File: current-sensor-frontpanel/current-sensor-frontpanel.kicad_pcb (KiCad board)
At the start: 2 copper layers, 98 x 30 mm, 8 parts

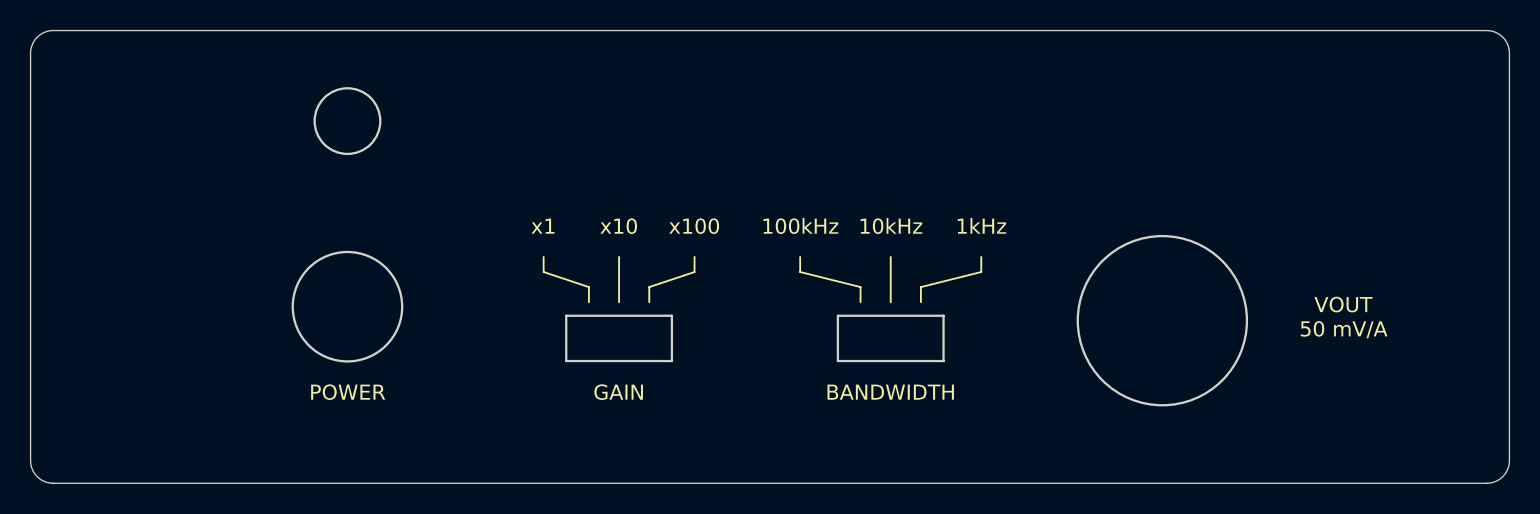
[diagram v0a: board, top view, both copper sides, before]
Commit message: complete front panel label
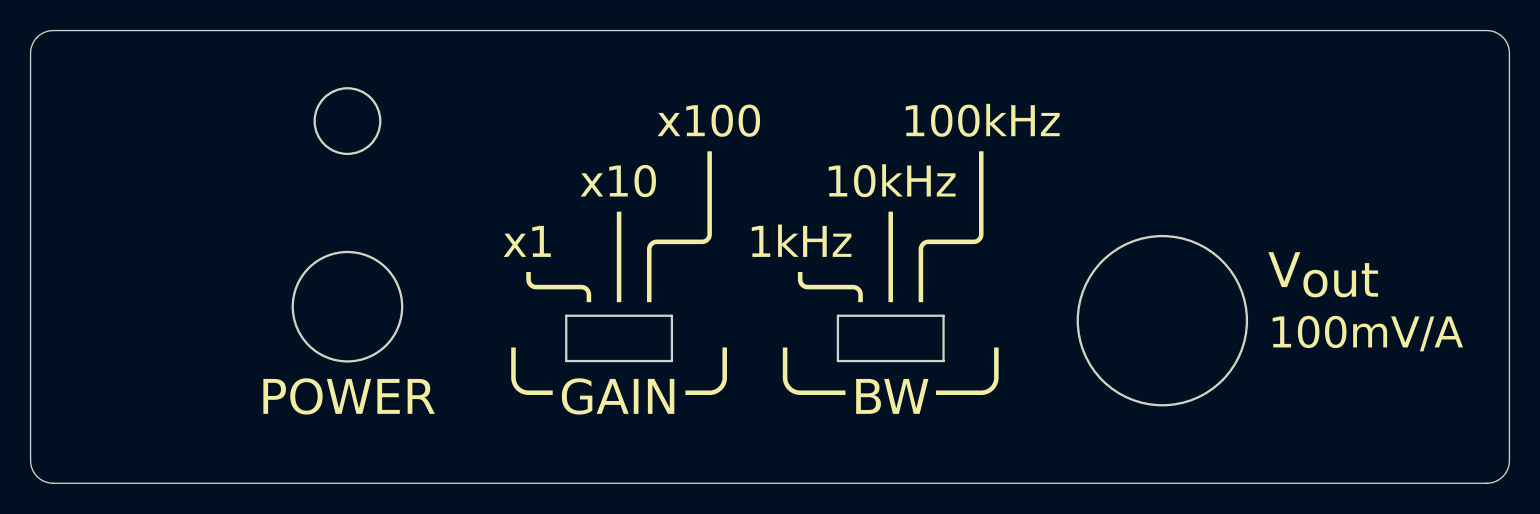
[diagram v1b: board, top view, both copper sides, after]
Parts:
- added C6: Front Panel Label, current-sensor:frontpanel, F.Cu at (100.0, 150.0)
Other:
- board text added: "Current Sensor Front Panel r0 G. Keeth github.com/gkeeth/current-sensor 2020-10-23"
- board text removed: "Current Sensor Front Panel r0 G. Keeth github.com/gkeeth/current-sensor 2020-08-13"
- board text removed: "VOUT 50 mV/A"
